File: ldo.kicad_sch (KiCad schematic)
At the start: 11 parts, among them U901 SE8633X2-HF, U902 SE8633X2-HF

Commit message: Move LDO schottkys to the input side
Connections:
- net +3V3: now also C904.1, D901.1 (K), TP902.1, U902.2 (VOUT); no longer D902.1 (K), D903.1 (K)
- net HS_Vin: now also D903.2 (A); no longer C901.1, U901.3 (VIN)
- net LS_Vin: now also D902.2 (A); no longer C902.1, U902.3 (VIN)
- removed net LLDO_OUT: C904.1, D902.2 (A), TP902.1, U902.2 (VOUT)
- new net: C902.1, D902.1 (K), U902.3 (VIN)
- new net: C901.1, D903.1 (K), U901.3 (VIN)
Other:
- note added: "Due to the schottky forward voltage drop, LS_Vin will always be preferred if both are available. If only HS_Vin is available, the output voltage will be lower than 3.3V."
- note removed: "Due to the diodes, output is actually less than 3.3V. If the host provides 3.3V, that is always preferred."
- note removed: "Due to two schottky forward voltage drops, LS_Vin will always be preferred if both are available."
- moved on the sheet: D902, D903
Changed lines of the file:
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@@
-    (stroke (width 0) (type default) (color 0 0 0 0))
-  )
-  (wire (pts (xy 149.86 101.6) (xy 154.94 101.6))
     (stroke (width 0) (type default) (color 0 0 0 0))
   )
   (wire (pts (xy 99.06 97.79) (xy 99.06 101.6))
+    (stroke (width 0) (type default) (color 0 0 0 0))
+  )
+  (wire (pts (xy 87.63 101.6) (xy 99.06 101.6))
+    (stroke (width 0) (type default) (color 0 0 0 0))
+  )
+  (wire (pts (xy 80.01 68.58) (xy 73.66 68.58))
     (stroke (width 0) (type default) (color 0 0 0 0))
   )
@@
     (stroke (width 0) (type default) (color 0 0 0 0))
   )
-  (wire (pts (xy 93.98 68.58) (xy 83.82 68.58))
+  (wire (pts (xy 93.98 68.58) (xy 87.63 68.58))
     (stroke (width 0) (type default) (color 0 0 0 0))
   )
-  (wire (pts (xy 124.46 101.6) (xy 142.24 101.6))
+  (wire (pts (xy 124.46 101.6) (xy 154.94 101.6))
     (stroke (width 0) (type default) (color 0 0 0 0))
   )
@@
     (stroke (width 0) (type default) (color 0 0 0 0))
   )
-  (wire (pts (xy 83.82 101.6) (xy 99.06 101.6))
+  (wire (pts (xy 73.66 101.6) (xy 80.01 101.6))
     (stroke (width 0) (type default) (color 0 0 0 0))
   )
@@
     (stroke (width 0) (type default) (color 0 0 0 0))
   )
-  (wire (pts (xy 154.94 68.58) (xy 152.4 68.58))
-    (stroke (width 0) (type default) (color 0 0 0 0))
-  )
   (wire (pts (xy 93.98 68.58) (xy 101.6 68.58))
     (stroke (width 0) (type default) (color 0 0 0 0))
@@
     (stroke (width 0) (type default) (color 0 0 0 0))
   )
-  (wire (pts (xy 144.78 68.58) (xy 140.97 68.58))
+  (wire (pts (xy 140.97 68.58) (xy 154.94 68.58))
     (stroke (width 0) (type default) (color 0 0 0 0))
   )
-  (text "Due to two schottky forward voltage drops,\nLS_Vin will always be preferred if both\nare available."
-    (at 132.08 58.42 0)
-    (effects (font (size 1.27 1.27)) (justify left bottom))
-  )
-  (text "Due to the diodes, output is\nactually less than 3.3V.\nIf the host provides 3.3V, that\nis always preferred."
-    (at 173.99 80.01 0)
+  (text "Due to the schottky forward voltage drop,\nLS_Vin will always be preferred if both\nare available.\n\nIf only HS_Vin is available, the output\nvoltage will be lower than 3.3V."
+    (at 146.05 63.5 0)
     (effects (font (size 1.27 1.27)) (justify left bottom))
   )
@@
     (effects (font (size 1.27 1.27)) (justify left bottom))
   )
-  (hierarchical_label "LS_Vin" (shape input) (at 83.82 101.6 180)
+  (hierarchical_label "LS_Vin" (shape input) (at 73.66 101.6 180)
     (effects (font (size 1.27 1.27)) (justify right))
   )
-  (hierarchical_label "HS_Vin" (shape input) (at 83.82 68.58 180)
+  (hierarchical_label "HS_Vin" (shape input) (at 73.66 68.58 180)
     (effects (font (size 1.27 1.27)) (justify right))
   )
@@
     (pin "2")
   )
-  (symbol (lib_id "Device:D_Schottky") (at 146.05 101.6 180) (unit 1)
+  (symbol (lib_id "Device:D_Schottky") (at 83.82 101.6 180) (unit 1)
     (in_bom yes) (on_board yes) (fields_autoplaced)
-    (property "Reference" "D902" (id 0) (at 146.3675 95.25 0))
-    (property "Value" "1N5819WS" (id 1) (at 146.3675 97.79 0))
-    (property "Footprint" "Diode_SMD:D_SOD-323" (id 2) (at 146.05 101.6 0)
+    (property "Reference" "D902" (id 0) (at 84.1375 95.25 0))
+    (property "Value" "1N5819WS" (id 1) (at 84.1375 97.79 0))
+    (property "Footprint" "Diode_SMD:D_SOD-323" (id 2) (at 83.82 101.6 0)
       (effects (font (size 1.27 1.27)) hide)
     )
-    (property "Datasheet" "~" (id 3) (at 146.05 101.6 0)
+    (property "Datasheet" "~" (id 3) (at 83.82 101.6 0)
       (effects (font (size 1.27 1.27)) hide)
     )
-    (property "LCSC" "C191023" (id 4) (at 146.05 101.6 0)
+    (property "LCSC" "C191023" (id 4) (at 83.82 101.6 0)
       (effects (font (size 1.27 1.27)) hide)
     )
@@
     (pin "2")
   )
-  (symbol (lib_id "Device:D_Schottky") (at 148.59 68.58 180) (unit 1)
+  (symbol (lib_id "Device:D_Schottky") (at 83.82 68.58 180) (unit 1)
     (in_bom yes) (on_board yes) (fields_autoplaced)
-    (property "Reference" "D903" (id 0) (at 148.9075 62.23 0))
-    (property "Value" "1N5819WS" (id 1) (at 148.9075 64.77 0))
-    (property "Footprint" "Diode_SMD:D_SOD-323" (id 2) (at 148.59 68.58 0)
+    (property "Reference" "D903" (id 0) (at 84.1375 62.23 0))
+    (property "Value" "1N5819WS" (id 1) (at 84.1375 64.77 0))
+    (property "Footprint" "Diode_SMD:D_SOD-323" (id 2) (at 83.82 68.58 0)
       (effects (font (size 1.27 1.27)) hide)
     )
-    (property "Datasheet" "~" (id 3) (at 148.59 68.58 0)
+    (property "Datasheet" "~" (id 3) (at 83.82 68.58 0)
       (effects (font (size 1.27 1.27)) hide)
     )
-    (property "LCSC" "C191023" (id 4) (at 148.59 68.58 0)
+    (property "LCSC" "C191023" (id 4) (at 83.82 68.58 0)
       (effects (font (size 1.27 1.27)) hide)
     )

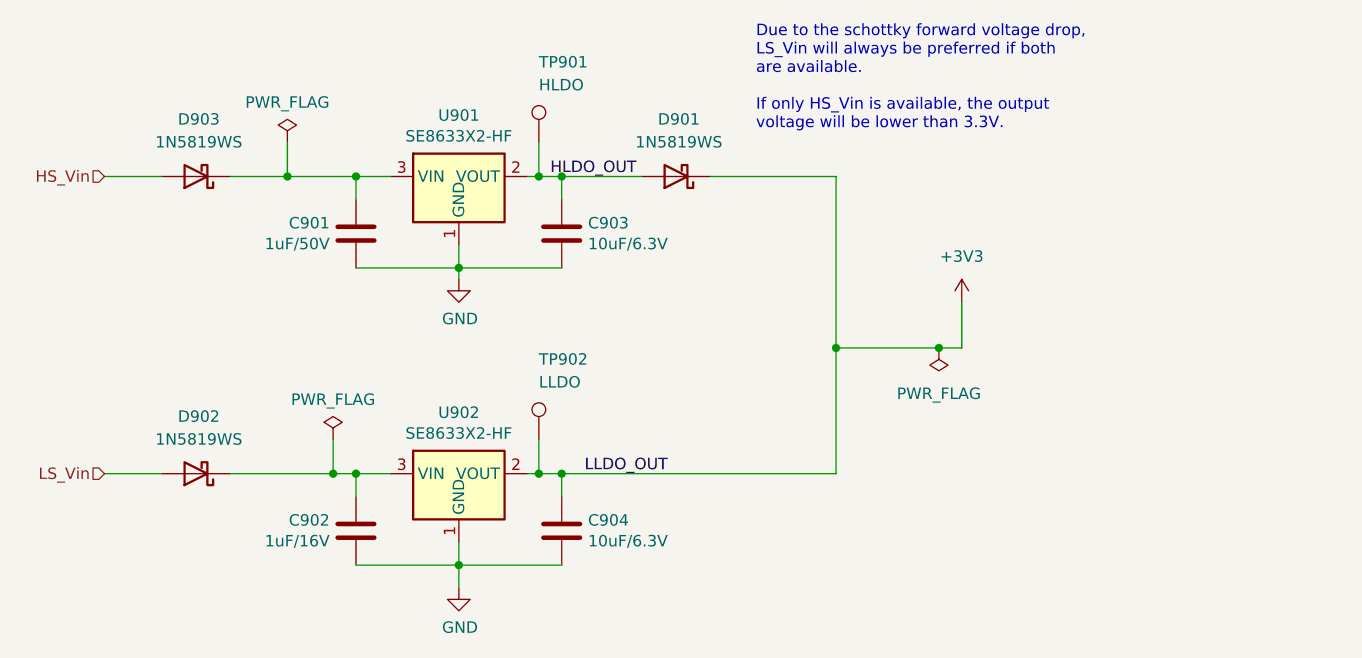
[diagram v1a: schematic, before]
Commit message: Tweak the layout and reroute tracks
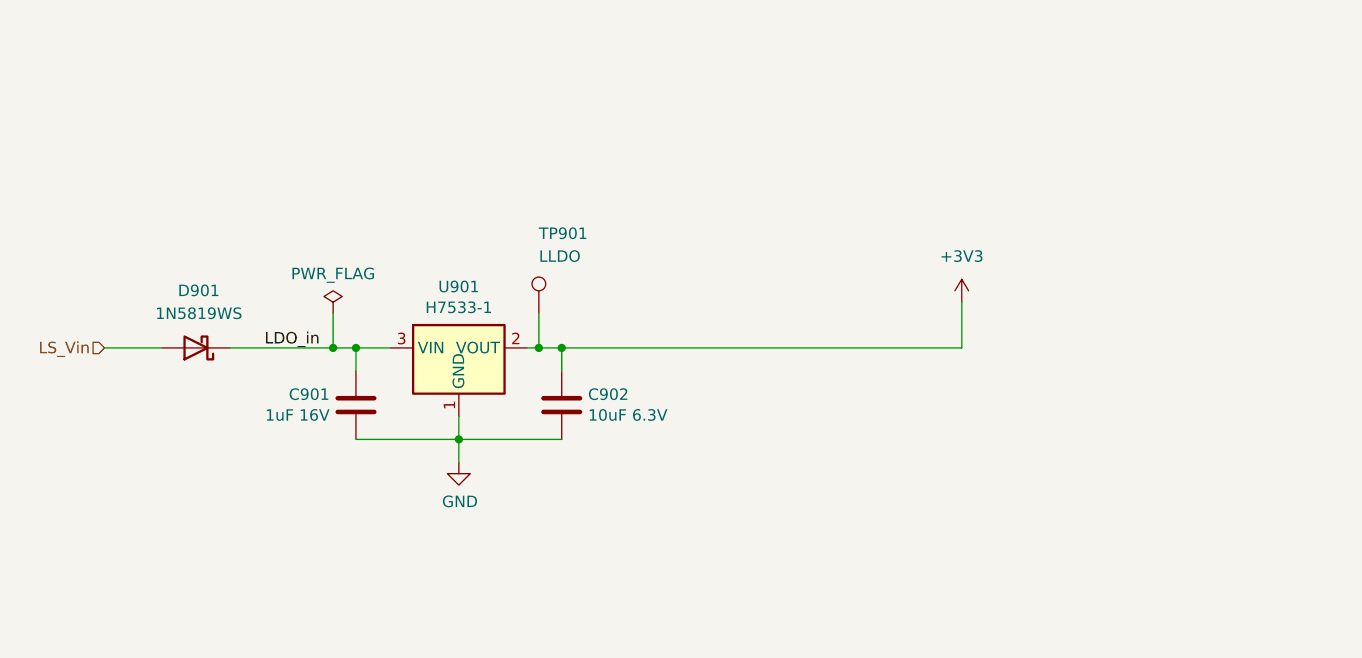
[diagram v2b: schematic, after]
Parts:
- removed C901: 1uF/50V, Capacitor_SMD:C_0805_2012Metric, symbol Device:C
- removed C903: 10uF/6.3V, Capacitor_SMD:C_0402_1005Metric, symbol Device:C
- removed D901, D903: 1N5819WS, Diode_SMD:D_SOD-323, symbol Device:D_Schottky
- removed TP901: HLDO, TestPoint:TestPoint_Pad_D2.0mm, symbol Connector:TestPoint
- removed U901: SE8633X2-HF, Package_TO_SOT_SMD:SOT-23, symbol SH-RPi:HT75xx-1-SOT23
- C901: renamed from C902; value 1uF/16V -> 1uF 16V
- C902: renamed from C904; value 10uF/6.3V -> 10uF 6.3V
- U901: renamed from U902; value SE8633X2-HF -> H7533-1; LCSC C496613 -> C277556
- renumbered D902 to D901, TP902 to TP901
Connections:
- net LDO_in: now reaches C901.1, D901.1 (K), U901.3 (VIN)
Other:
- note removed: "Due to the schottky forward voltage drop, LS_Vin will always be preferred if both are available. If only HS_Vin is available, the output voltage will be lower than 3.3V."
- moved on the sheet: C901, C902, D901, TP901, U901

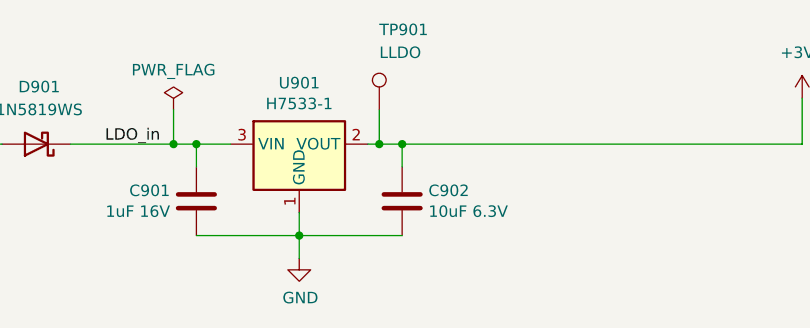
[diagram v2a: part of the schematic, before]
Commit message: Add test points, test footprints, GND vias
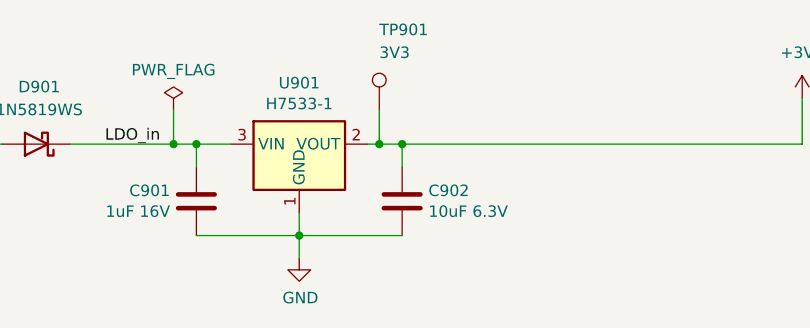
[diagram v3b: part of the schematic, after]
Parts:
- TP901: value LLDO -> 3V3
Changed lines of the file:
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@@
       (effects (font (size 1.27 1.27)) (justify left))
     )
-    (property "Value" "LLDO" (id 1) (at 121.92 77.47 0)
+    (property "Value" "3V3" (id 1) (at 121.92 77.47 0)
       (effects (font (size 1.27 1.27)) (justify left))
     )
